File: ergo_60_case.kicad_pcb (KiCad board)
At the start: 2 copper layers, 285 x 94.6 mm, 163 parts, among them SW1 SW_Push, U1 PRTR5V0U2X, U2 OLED_SSD1306, U3 AT90USB1286-AU, U4 AVR-ISP, Y1 16MHz

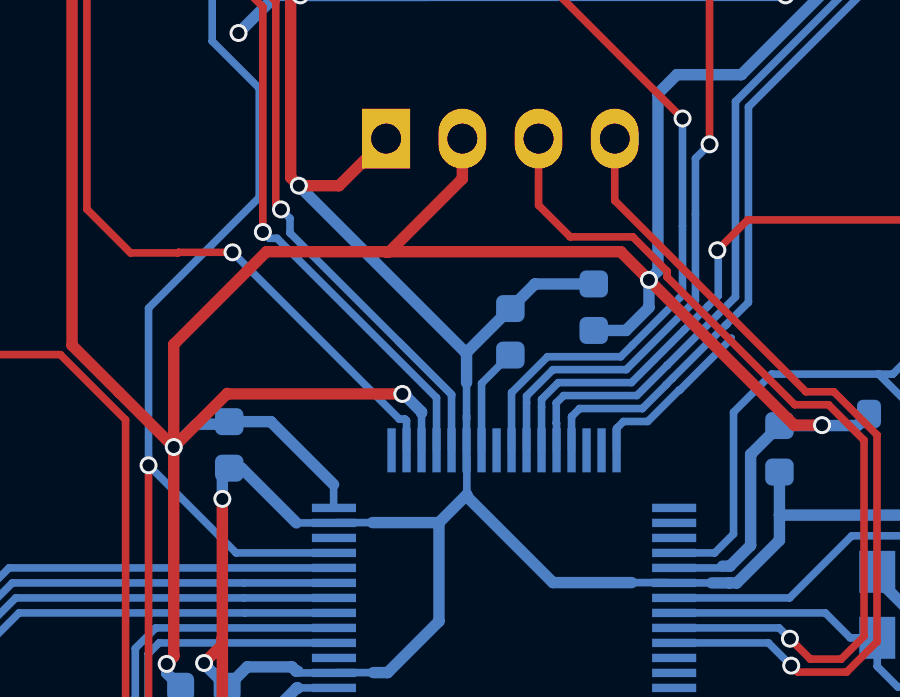
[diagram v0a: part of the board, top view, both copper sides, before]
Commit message: corrected mising +5v trace and funky looking schematic on led 56
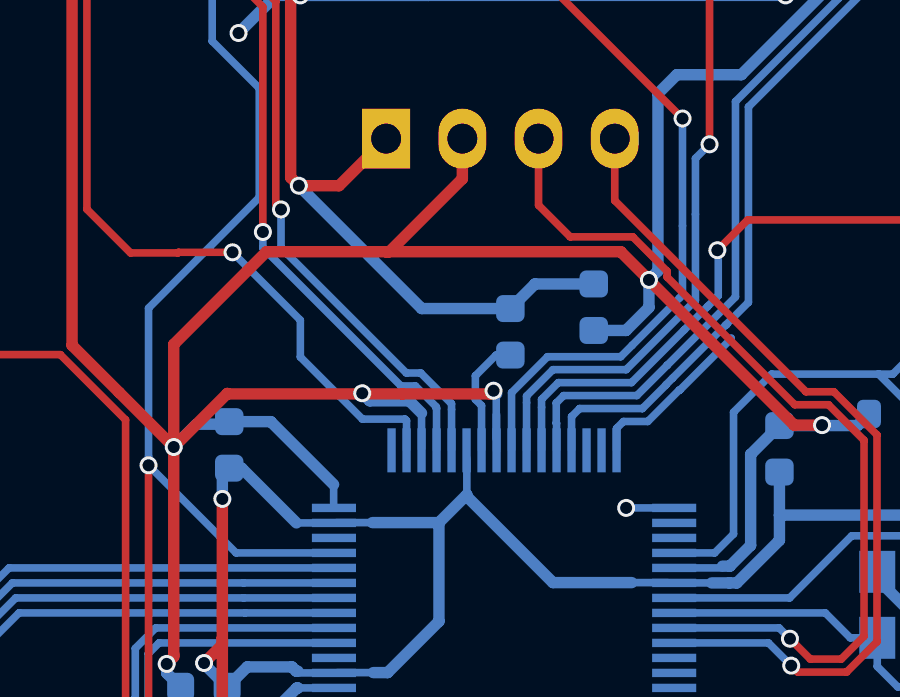
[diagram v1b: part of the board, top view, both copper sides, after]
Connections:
- D56 pad 1: Net-(D55-Pad1) -> Net-(D56-Pad1)
- D57 pad 3: Net-(D55-Pad1) -> Net-(D56-Pad1)
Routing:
- net Net-(D55-Pad1): track 42.3 -> 24.2 mm
- net Net-(D56-Pad1): track 0.00 -> 18.2 mm
- net +5V: track 266.5 -> 273.8 mm, vias 6 -> 7
- net GND: track 1302.8 -> 1298.1 mm
- net D+: track 170.5 -> 168.3 mm
- net Net-(U3-Pad17): track 0.00 -> 1.60 mm, vias 0 -> 1
- net LEDDATA: track 165.3 -> 166.1 mm

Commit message: updates for prod
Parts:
- U2: footprint KiCadLibs:SSD1306_128x64OLED_wHoles -> KiCadLibs:SSD1306_128x64OLED
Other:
- rule pad_to_mask_clearance: 0 -> 0.05

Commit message: correct mcu processor footprint
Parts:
- added G***: LOGO, KiCadImages:FlyingMX_largesilk, F.Cu at (324.5, 97.6)
- added G***: LOGO, KiCadImages:GearLogo_smallsolder, F.Cu at (270.5, 159.3)
- added LED1: LED_Strip, KiCadLibs:StripLED, F.Cu at (193.0, 97.8)
- added LED2: LED_Strip, KiCadLibs:StripLED_BackOnly, F.Cu at (72.8, 125.5)
- added LED3: LED_Strip, KiCadLibs:StripLED, F.Cu at (194.6, 157.0)
- U2: footprint KiCadLibs:SSD1306_128x64OLED -> KiCadLibs:SSD1306_128x64OLED_wHoles
- U3: footprint KiCadLibs:AT90USB1286-AUQFP50P1200X1200X120-64N -> KiCadLibs:AT90USB1286-AU_QFP80P1600X1600X120-64N
- moved RC7 2.52 mm to (204.5, 146.4)
- moved C3 2.46 mm to (206.2, 123.5)
- moved C7 2.44 mm to (217.7, 129.6)
- moved C6 2.13 mm to (208.9, 123.1)
- moved RC5 1.63 mm to (220.7, 128.8)
- moved C4 1.55 mm to (196.3, 128.4)
- moved C5 0.58 mm to (195.6, 138.2)
- moved D1 0.15 mm to (75.4, 141.0)
- moved D51 0.13 mm to (307.4, 147.0)
- moved D52 0.12 mm to (326.8, 150.1)
- moved D6 0.11 mm to (171.3, 137.4)
- moved D8 0.11 mm to (230.2, 138.3)
- moved D41 0.10 mm to (94.0, 146.1)
- moved D4 0.10 mm to (133.8, 128.6)
- moved D13 0.10 mm to (326.1, 142.0)
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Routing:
- net LEDDATA: track 166.1 -> 267.6 mm, vias 4 -> 11
- net VCC: track 827.0 -> 870.9 mm, vias 5 -> 7
- net GND: track 1298.0 -> 1337.5 mm, vias 20 -> 21
- net +5V: track 273.8 -> 266.4 mm, vias 7 -> 6
- net COL0: track 220.8 -> 213.6 mm
- net Net-(U3-Pad16): track 5.82 -> 0.00 mm
- net COL7: track 88.6 -> 85.6 mm
- net COL8: track 114.4 -> 111.5 mm
- net COL2: track 175.4 -> 172.5 mm
- net COL3: track 155.8 -> 153.0 mm
- net COL1: track 198.0 -> 195.3 mm
- net MOSI: track 26.7 -> 24.1 mm
- net MISO: track 29.9 -> 27.6 mm
- net XTAL2: track 14.0 -> 11.8 mm
- net COL9: track 137.1 -> 134.9 mm
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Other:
- board text added: "EIN60_Prototype"
- board text added: "klackygears"

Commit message: smooth routing?
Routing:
- net GND: track 1337.5 -> 1351.0 mm
- net VCC: track 870.9 -> 876.0 mm
- net RESET: track 196.5 -> 192.0 mm
- net ROW1: track 319.4 -> 317.2 mm
- net ROW3: track 304.2 -> 302.0 mm
- net Net-(D39-Pad2): track 20.4 -> 22.0 mm
- net Net-(D46-Pad2): track 15.3 -> 13.8 mm
- net ROW2: track 303.9 -> 302.3 mm
- net COL11: track 176.1 -> 174.6 mm
- net Net-(D51-Pad2): track 10.6 -> 12.0 mm
- net ROT3: track 37.9 -> 36.6 mm
- net COL12: track 197.4 -> 196.1 mm
- net COL10: track 156.0 -> 154.9 mm
- net COL9: track 134.9 -> 133.7 mm
- net Net-(D50-Pad2): track 10.6 -> 11.6 mm
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
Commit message: progress
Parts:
- removed G***: LOGO, KiCadImages:FlyingMX_largesilk
- removed G***: LOGO, KiCadImages:GearLogo_smallsolder
- moved C10 2.40 mm to (208.3, 149.1)
- moved C11 1.02 mm to (212.5, 150.7)
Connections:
- U3 pad 35: Net-(U3-Pad35) -> COL9
- U3 pad 36: Net-(U3-Pad36) -> COL10
- U3 pad 37: COL9 -> COL11
- U3 pad 38: COL10 -> COL12
- U3 pad 39: COL11 -> ROT3
- U3 pad 40: COL12 -> ROT2
- U3 pad 41: ROT3 -> Net-(U3-Pad41)
- U3 pad 42: ROT2 -> Net-(U3-Pad42)
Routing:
- net LEDDATA: track 266.6 -> 257.4 mm
- net COL12: track 196.1 -> 187.3 mm
- net ROW1: track 317.2 -> 308.8 mm
- net VCC: track 876.0 -> 883.1 mm
- net COL11: track 174.6 -> 167.7 mm
- net ROW0: track 401.2 -> 394.5 mm
- net D+: track 165.9 -> 160.4 mm
- net +5V: track 266.3 -> 260.8 mm
- net D-: track 165.5 -> 160.1 mm
- net COL0: track 213.6 -> 208.6 mm
- net ROW2: track 302.3 -> 298.2 mm
- net COL10: track 154.9 -> 151.2 mm
- net ROW3: track 302.0 -> 298.3 mm
- net COL1: track 194.6 -> 191.0 mm
- net COL9: track 133.7 -> 130.4 mm
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- removed copper zone on F.Cu, net GND
